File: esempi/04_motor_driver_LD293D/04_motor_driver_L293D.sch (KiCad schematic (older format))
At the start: 20 parts, among them IC1 L293D, P1 MOTOR1_DIRECTION, P2 MOTOR1_ENABLE, P3 CONN_01X02, P4 MOTOR2_ENABLE, P5 CONN_01X02, P6 MOTOR2_DIRECTION, P7 CONN_01X01, P8 CONN_01X01, P9 CONN_01X01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

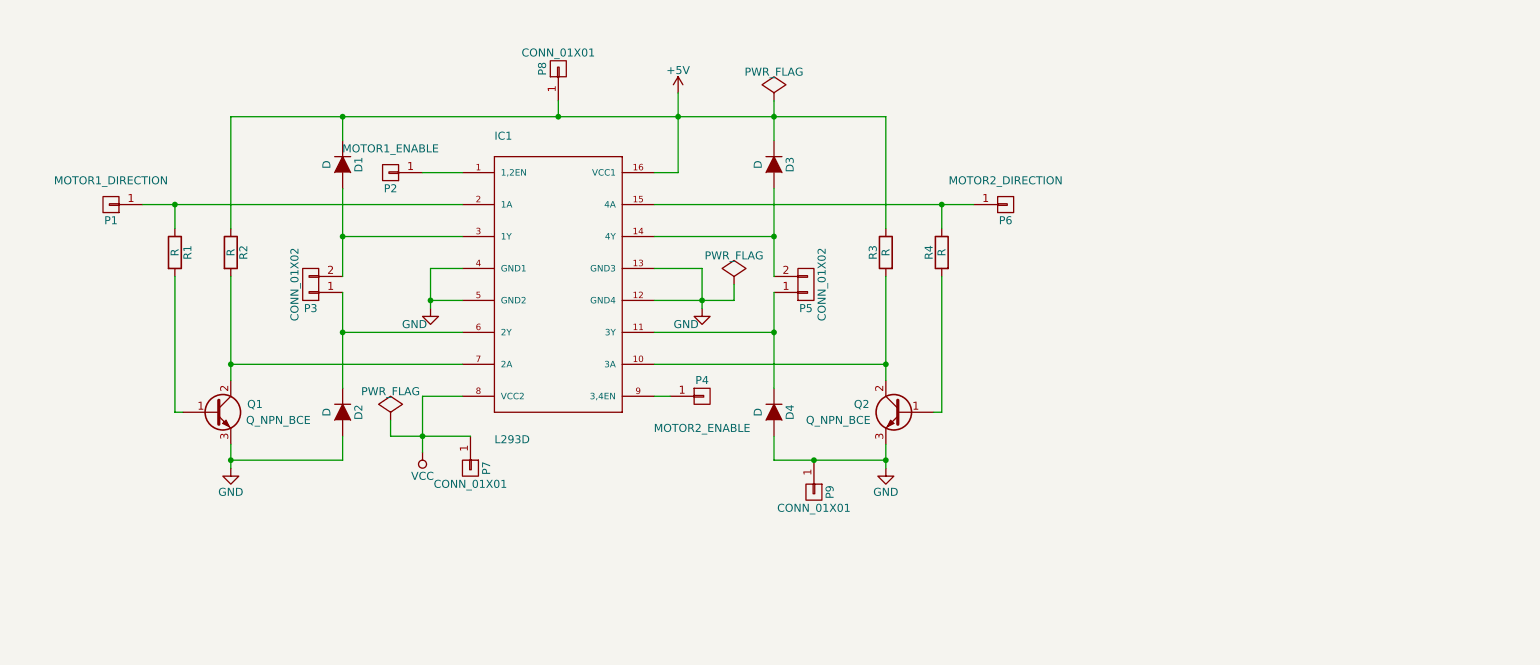
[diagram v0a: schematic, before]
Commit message: sistemato circuito L293D aggiunti 2 diodi mancanti
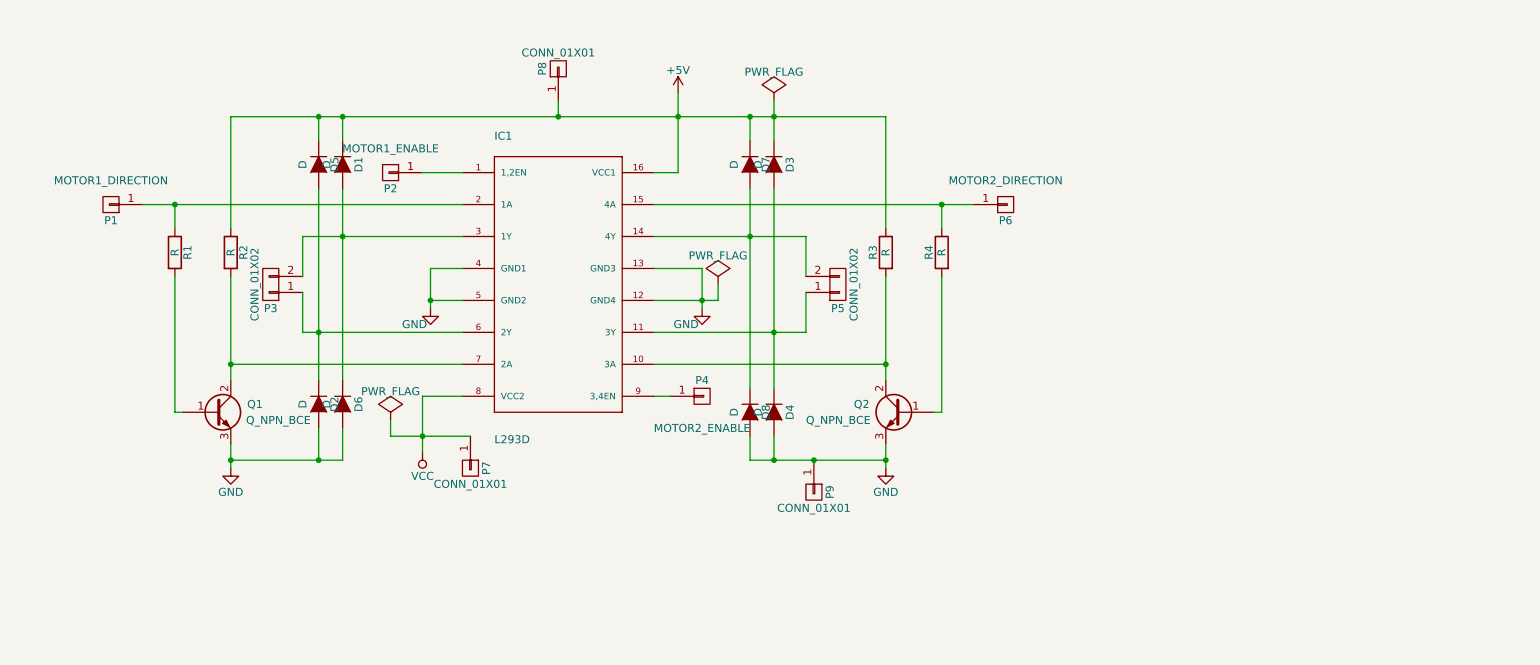
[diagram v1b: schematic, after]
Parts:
- added D5, D6, D7, D8: D, w_pth_diodes:diode_do35, symbol D
- R1, R2, R3, R4: footprint w_pth_resistors:R12x5.2 -> w_pth_resistors:RC03
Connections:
- net +5V: now also D5.1 (K), D7.1 (K)
- net GND: now also D6.2 (A), D8.2 (A)
- net at D4.1 (K), IC1.11 (3Y), P5.1 (P1): now also D3.2 (A)
- net at IC1.14 (4Y), P5.2 (P2): now also D7.2 (A), D8.1 (K); no longer D3.2 (A)
- net at D1.2 (A), IC1.3 (1Y), P3.2 (P2): now also D6.1 (K)
- net at D2.1 (K), IC1.6 (2Y), P3.1 (P1): now also D5.2 (A)
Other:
- moved on the sheet: D2, P3, P5

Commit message: Modifiche alla board per uso su motori recuperati da macchinetta caffe
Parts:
- removed P1: MOTOR1_DIRECTION, w_pin_strip:pin_strip_1, symbol CONN_01X01
- removed P2: MOTOR1_ENABLE, w_pin_strip:pin_strip_1, symbol CONN_01X01
- removed P4: MOTOR2_ENABLE, w_pin_strip:pin_strip_1, symbol CONN_01X01
- removed P8, P9: CONN_01X01, w_pin_strip:pin_strip_1, symbol CONN_01X01
- added J1: Arduino_Nano_Header, w_conn_misc:arduino_nano_header, symbol Arduino_Nano_Header
- added P2: ALIM_HALL, w_pin_strip:pin_strip_6, symbol CONN_01X06
- added P3: MOTOR_CTR, w_pin_strip:pin_strip_4, symbol CONN_01X04
- added P5: HALL_01, w_pin_strip:pin_strip_2mm_3, symbol CONN_01X03
- added P8: HALL_02, w_pin_strip:pin_strip_2mm_3, symbol CONN_01X03
- added P9: ING5V, w_pin_strip:pin_strip_2, symbol CONN_01X02
- D1: renamed from D5; footprint w_pth_diodes:diode_do35 -> w_smd_diode:sod123
- D2: footprint w_pth_diodes:diode_do35 -> w_smd_diode:sod123
- D3: renamed from D1; footprint w_pth_diodes:diode_do35 -> w_smd_diode:sod123
- D4: renamed from D6; footprint w_pth_diodes:diode_do35 -> w_smd_diode:sod123
- D5: renamed from D7; footprint w_pth_diodes:diode_do35 -> w_smd_diode:sod123
- D6: renamed from D8; footprint w_pth_diodes:diode_do35 -> w_smd_diode:sod123
- D7: renamed from D3; footprint w_pth_diodes:diode_do35 -> w_smd_diode:sod123
- D8: renamed from D4; footprint w_pth_diodes:diode_do35 -> w_smd_diode:sod123
- P1: renamed from P3; value CONN_01X02 -> OUT12
- P4: renamed from P5; value CONN_01X02 -> OUT34
- P6: value MOTOR2_DIRECTION -> HOLE1; footprint w_pin_strip:pin_strip_1 -> w_details:hole_3mm5
- P7: value CONN_01X01 -> HOLE2; footprint w_pin_strip:pin_strip_1 -> w_details:hole_3mm5
- Q1, Q2: symbol Q_NPN_BCE -> Q_NPN_BCE-RESCUE-04_motor_driver_L293D
- R1, R2, R3, R4: footprint w_pth_resistors:RC03 -> w_smd_resistors:r_0805
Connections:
- net +5V: now also J1.27 (5V), P2.4 (P4), P5.1 (P1), P8.1 (P1), P9.2 (P2)
- net GND: now also J1.29 (GND), P2.1 (P1), P2.2 (P2), P5.2 (P2), P8.2 (P2), P9.1 (P1)
- net VCC: now also P2.3 (P3); no longer P7.1 (P1)
- net 1,2EN: now reaches IC1.1 (1,2EN)
- net 1,2EN: now also J1.9 (D6/AIN0), P3.4 (P4)
- net 3,4DIR: now reaches IC1.15 (4A), R4.1
- net 3,4DIR: now also J1.8 (D5/T1), P3.1 (P1); no longer P6.1 (P1)
- net 1,2DIR: now reaches IC1.2 (1A), R1.1
- net 1,2DIR: now also J1.7 (D4/T0), P3.2 (P2)
- net 3,4EN: now reaches IC1.9 (3,4EN)
- net 3,4EN: now also J1.10 (D7/AIN1), P3.3 (P3)
- new net: J1.19 (A0), P2.5 (P5), P5.3 (P3)
- new net: J1.20 (A1), P2.6 (P6), P8.3 (P3)
- no-connect marks 0 -> 24
